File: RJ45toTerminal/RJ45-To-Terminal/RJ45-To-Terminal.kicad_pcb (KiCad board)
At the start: 2 copper layers, 69.5 x 58.1 mm, 71 parts, among them J11 Screw_Terminal_01x08, J12 Screw_Terminal_01x08, J13 Screw_Terminal_01x08, J14 Screw_Terminal_01x08

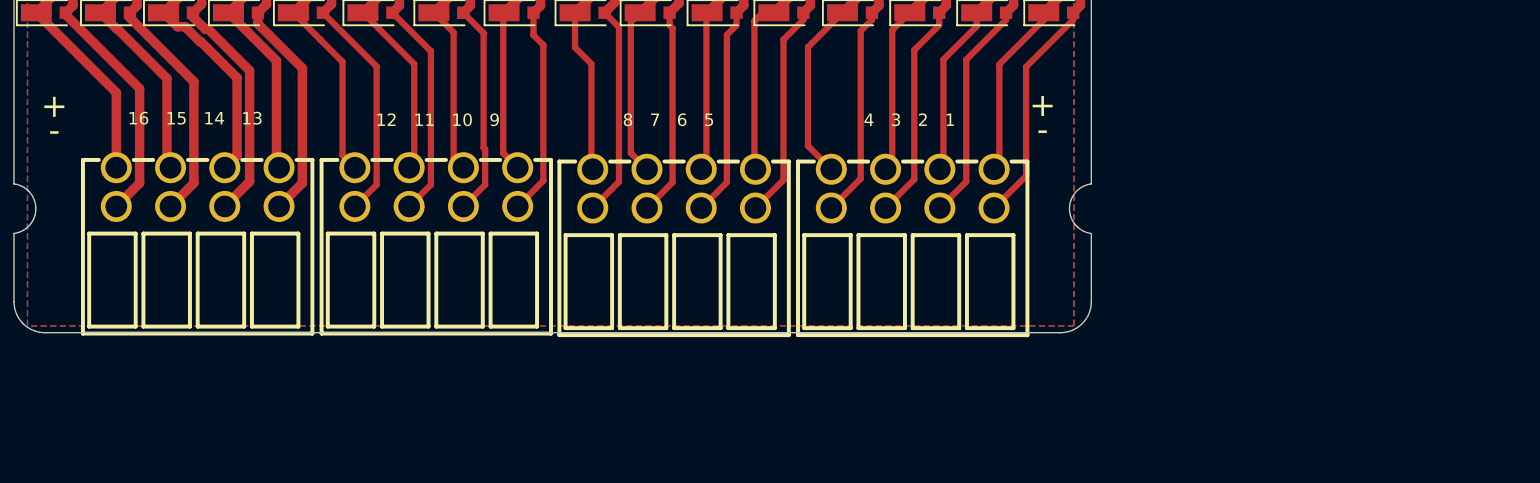
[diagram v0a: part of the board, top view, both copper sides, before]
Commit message: read me update and label
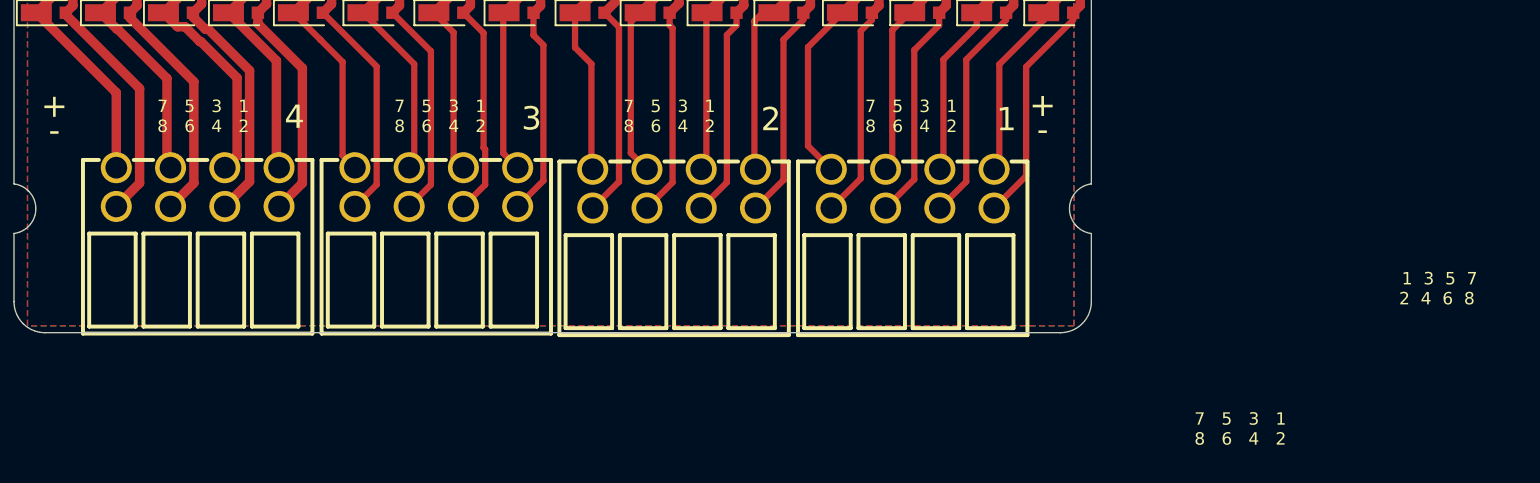
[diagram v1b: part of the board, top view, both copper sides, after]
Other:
- board text added: "1 3 5 7 2 4 6 8"
- board text added: "7 5 3 1 8 6 4 2"
- board text removed: "12 11 10 9"
- board text removed: "16 15 14 13"
- board text removed: "4 3 2 1"
- board text removed: "8 7 6 5"
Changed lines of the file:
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@@
     (effects (font (size 1.180592 1.180592) (thickness 0.241808)) (justify left bottom mirror))
   )
-  (gr_text "4   3   2   1" (at 172.6692 106.3752) (layer "F.SilkS")
-    (effects (font (size 0.8 0.8) (thickness 0.2)))
+  (gr_text "3" (at 148.2852 106.2736) (layer "F.SilkS")
+    (effects (font (size 1.5 1.5) (thickness 0.3)))
   )
   (gr_text "4" (at 133.5532 85.344) (layer "F.SilkS")
@@
     (effects (font (size 1.5 1.5) (thickness 0.3)))
   )
-  (gr_text "16   15   14   13" (at 126.5936 106.2736) (layer "F.SilkS")
-    (effects (font (size 0.8 0.8) (thickness 0.2)))
-  )
   (gr_text "+" (at 117.5004 105.4608) (layer "F.SilkS")
     (effects (font (size 1.5 1.5) (thickness 0.3)))
   )
-  (gr_text "12   11   10   9" (at 142.24 106.3752) (layer "F.SilkS")
+  (gr_text "7   5   3   1\n8   6   4   2" (at 194.0052 126.2888) (layer "F.SilkS")
+    (effects (font (size 0.8 0.8) (thickness 0.2)))
+  )
+  (gr_text "7   5   3   1\n8   6   4   2" (at 142.3924 106.1212) (layer "F.SilkS")
+    (effects (font (size 0.8 0.8) (thickness 0.2)))
+  )
+  (gr_text "7   5   3   1\n8   6   4   2" (at 172.7708 106.1212) (layer "F.SilkS")
     (effects (font (size 0.8 0.8) (thickness 0.2)))
   )
@@
     (effects (font (size 1.5 1.5) (thickness 0.3)))
   )
+  (gr_text "7   5   3   1\n8   6   4   2" (at 127.1016 106.1212) (layer "F.SilkS")
+    (effects (font (size 0.8 0.8) (thickness 0.2)))
+  )
   (gr_text "+" (at 181.2544 105.41) (layer "F.SilkS")
+    (effects (font (size 1.5 1.5) (thickness 0.3)))
+  )
+  (gr_text "1" (at 178.9176 106.3244) (layer "F.SilkS")
     (effects (font (size 1.5 1.5) (thickness 0.3)))
   )
@@
     (effects (font (size 1.5 1.5) (thickness 0.3)))
   )
-  (gr_text "8   7   6   5" (at 157.1244 106.3752) (layer "F.SilkS")
+  (gr_text "1" (at 178.7144 85.4456) (layer "F.SilkS")
+    (effects (font (size 1.5 1.5) (thickness 0.3)))
+  )
+  (gr_text "7   5   3   1\n8   6   4   2" (at 157.1752 106.1212) (layer "F.SilkS")
     (effects (font (size 0.8 0.8) (thickness 0.2)))
   )
-  (gr_text "1" (at 178.7144 85.4456) (layer "F.SilkS")
-    (effects (font (size 1.5 1.5) (thickness 0.3)))
+  (gr_text "   1  3  5  7 \n  2  4  6  8" (at 206.33772 117.238601) (layer "F.SilkS")
+    (effects (font (size 0.8 0.8) (thickness 0.2)))
   )
   (gr_text "3" (at 147.3708 85.344) (layer "F.SilkS")
     (effects (font (size 1.5 1.5) (thickness 0.3)))
   )
+  (gr_text "4" (at 132.9944 106.172) (layer "F.SilkS")
+    (effects (font (size 1.5 1.5) (thickness 0.3)))
+  )
+  (gr_text "2" (at 163.7284 106.3244) (layer "F.SilkS")
+    (effects (font (size 1.5 1.5) (thickness 0.3)))
+  )

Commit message: documents
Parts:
- removed the G*** at (194.7, 50.1)
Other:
- board text removed: "1 3 5 7 2 4 6 8"
- board text removed: "1: Data 1 2: Data 2 3: Data 3 4: VIN 5: VIN 6: Data 4 7: GND 8: GND"
- board text removed: "Copyright 2019-2021 SuperHouse Automation Pty Ltd Released under the terms of the TAPR Open Hardware License: www.tapr.org/OHL"
- board text removed: "Passive POE Injector v0.1 2023"
- board text removed: "RJ45 Pinout"
- board text removed: "www.superhouse.tv/i2crj45"
